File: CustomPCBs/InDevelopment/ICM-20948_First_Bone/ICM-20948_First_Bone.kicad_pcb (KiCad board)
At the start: 4 copper layers, 7 x 10.1 mm, 14 parts, among them J1 Conn_01x04_MountingPin, T1 BSS138BKS_115, U1 ICM-20948, U2 HE6206-18NR

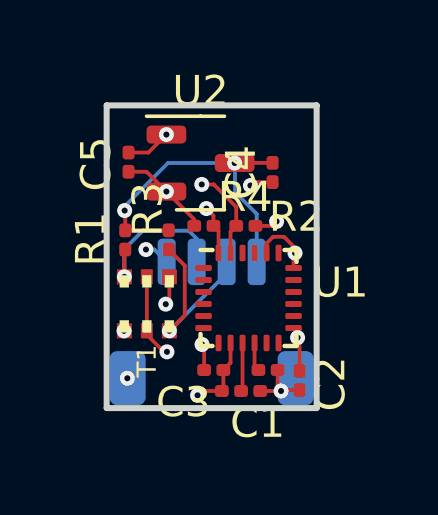
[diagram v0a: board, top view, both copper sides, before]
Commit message: BMI160+mag board finished, fixed CS on ICM-20948
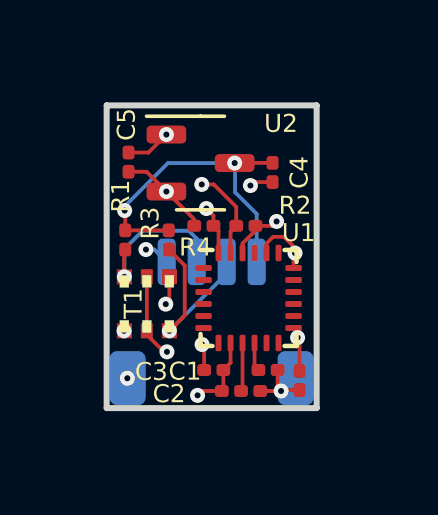
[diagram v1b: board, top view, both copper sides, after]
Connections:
- U1 pad 22: unconnected-(U1-~{CS}-Pad22) -> +1V8
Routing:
- net +1V8: track 10.8 -> 11.9 mm
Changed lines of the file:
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@@
   (net 23 "unconnected-(U1-RESV-Pad19)")
   (net 24 "unconnected-(U1-AUX_DA-Pad21)")
-  (net 25 "unconnected-(U1-~{CS}-Pad22)")
   (footprint "Capacitor_SMD:C_0201_0603Metric" (layer "F.Cu")
     (at 100.07 101.605)
@@
     (property "ki_keywords" "cap capacitor")
     (attr smd)
-    (fp_text reference "C3" (at -1.01 1.075) (layer "F.SilkS")
-        (effects (font (size 1 1) (thickness 0.15)))
+    (fp_text reference "C3" (at -2.08 0.055) (layer "F.SilkS")
+        (effects (font (size 0.6 0.6) (thickness 0.15)))
     )
     (fp_text value "100n" (at 0 1.05) (layer "F.Fab")
@@
     (property "ki_keywords" "R res resistor")
     (attr smd)
-    (fp_text reference "R1" (at -0.03 1.14 90) (layer "F.SilkS")
-        (effects (font (size 1 1) (thickness 0.15)))
+    (fp_text reference "R1" (at -1.46 0.15 90) (layer "F.SilkS")
+        (effects (font (size 0.6 0.6) (thickness 0.15)))
     )
     (fp_text value "10k" (at 0 1.05 90) (layer "F.Fab")
@@
     (property "ki_keywords" "R res resistor")
     (attr smd)
-    (fp_text reference "R4" (at 1.38 -0.96) (layer "F.SilkS")
-        (effects (font (size 1 1) (thickness 0.15)))
+    (fp_text reference "R4" (at -0.28 0.71) (layer "F.SilkS")
+        (effects (font (size 0.6 0.6) (thickness 0.15)))
     )
     (fp_text value "10k" (at 0 1.05) (layer "F.Fab")
@@
     (property "ki_keywords" "R res resistor")
     (attr smd)
-    (fp_text reference "R2" (at -1.68 0.3) (layer "F.SilkS")
-        (effects (font (size 1 1) (thickness 0.15)))
+    (fp_text reference "R2" (at -1.64 0.68) (layer "F.SilkS")
+        (effects (font (size 0.6 0.6) (thickness 0.15)))
     )
     (fp_text value "10k" (at 0 1.05) (layer "F.Fab")
@@
     (property "ki_keywords" "cap capacitor")
     (attr smd)
-    (fp_text reference "C2" (at 0.115 -1.03 90) (layer "F.SilkS")
-        (effects (font (size 1 1) (thickness 0.15)))
+    (fp_text reference "C2" (at 0.445 4.35 -180) (layer "F.SilkS")
+        (effects (font (size 0.6 0.6) (thickness 0.15)))
     )
     (fp_text value "100n" (at 0 1.05 90) (layer "F.Fab")
@@
     (property "ki_keywords" "mems magnetometer")
     (attr smd)
-    (fp_text reference "U1" (at 3.06 -0.51) (layer "F.SilkS")
-        (effects (font (size 1 1) (thickness 0.15)))
+    (fp_text reference "U1" (at 1.67 -2.175) (layer "F.SilkS")
+        (effects (font (size 0.6 0.6) (thickness 0.15)))
     )
     (fp_text value "ICM-20948" (at 0 3.25) (layer "F.Fab")
@@
       (net 24 "unconnected-(U1-AUX_DA-Pad21)") (pinfunction "AUX_DA") (pintype "bidirectional"))
     (pad "22" smd roundrect (at -0.2 -1.5 90) (size 0.55 0.2) (layers "F.Cu" "F.Paste" "F.Mask") (roundrect_rratio 0.25)
-      (net 25 "unconnected-(U1-~{CS}-Pad22)") (pinfunction "~{CS}") (pintype "input"))
+      (net 3 "+1V8") (pinfunction "~{CS}") (pintype "input"))
     (pad "23" smd roundrect (at -0.6 -1.5 90) (size 0.55 0.2) (layers "F.Cu" "F.Paste" "F.Mask") (roundrect_rratio 0.25)
       (net 7 "SCL_1V8") (pinfunction "SCL/SCLK") (pintype "input"))
@@
       )
     )
-    (model "${KICAD6_3DMODEL_DIR}/Package_DFN_QFN.3dshapes/QFN-24_3x3mm_P0.4mm_EP1.7x1.54mm.wrl"
-      (offset (xyz 0 0 0))
-      (scale (xyz 1 1 1))
-      (rotate (xyz 0 0 0))
+    (model ":REPO_ROOT:CustomPCBs/ComponentLibraries/3dmodels/ICM-20948.step"
+      (offset (xyz 0 0 0))
+      (scale (xyz 1 1 1))
+      (rotate (xyz -90 0 0))
     )
   )
@@
     (property "ki_keywords" "Torex LDO Voltage Regulator Fixed Positive")
     (attr smd)
-    (fp_text reference "U2" (at 0 -2.4) (layer "F.SilkS")
-        (effects (font (size 1 1) (thickness 0.15)))
+    (fp_text reference "U2" (at 2.68075 -1.31675) (layer "F.SilkS")
+        (effects (font (size 0.6 0.6) (thickness 0.15)))
     )
     (fp_text value "HE6206-18NR" (at 0 2.4) (layer "F.Fab")
@@
     (pad "3" smd roundrect (at 1.1375 0) (size 1.325 0.6) (layers "F.Cu" "F.Paste" "F.Mask") (roundrect_rratio 0.25)
       (net 4 "+3.3V") (pinfunction "VI") (pintype "power_in"))
-    (model "${KICAD6_3DMODEL_DIR}/Package_TO_SOT_SMD.3dshapes/SOT-23-3.wrl"
-      (offset (xyz 0 0 0))
-      (scale (xyz 1 1 1))
-      (rotate (xyz 0 0 0))
+    (model ":REPO_ROOT:CustomPCBs/ComponentLibraries/3dmodels/User Library-SOT23-3.step"
+      (offset (xyz 0 0 0))
+      (scale (xyz 1 1 1))
+      (rotate (xyz 0 0 90))
     )
   )
@@
     (property "ki_keywords" "cap capacitor")
     (attr smd)
-    (fp_text reference "C5" (at 0.06 1.08 90) (layer "F.SilkS")
-        (effects (font (size 1 1) (thickness 0.15)))
+    (fp_text reference "C5" (at -1.25675 0.06925 90) (layer "F.SilkS")
+        (effects (font (size 0.6 0.6) (thickness 0.15)))
     )
     (fp_text value "1u" (at 0 1.05 90) (layer "F.Fab")
@@
     (property "SnapEDA_Link" "https://www.snapeda.com/parts/BSS138BKS,115/Nexperia/view-part/?ref=snap")
     (attr smd)
-    (fp_text reference "T1" (at -1.90803 0 90) (layer "F.SilkS")
-        (effects (font (size 0.641017 0.641017) (thickness 0.15)))
+    (fp_text reference "T1" (at 0.01 -0.45 90) (layer "F.SilkS")
+        (effects (font (size 0.6 0.6) (thickness 0.15)))
     )
     (fp_text value "BSS138BKS_115" (at 1.90726 0 90) (layer "F.Fab")
@@
     (pad "6" smd roundrect (at 0.9 -0.75) (size 0.5 0.5) (layers "F.Cu" "F.Paste" "F.Mask") (roundrect_rratio 0.03)
       (net 6 "SCL") (pintype "passive") (solder_mask_margin 0.102))
+    (model ":REPO_ROOT:CustomPCBs/ComponentLibraries/3dmodels/User Library-TSSOP-6 (SOT-23-6 PITCH 0_65).STEP"
+      (offset (xyz 0 0 0.75))
+      (scale (xyz 1 1 1))
+      (rotate (xyz 0 0 -90))
+    )
   )
   (footprint "Resistor_SMD:R_0201_0603Metric" (layer "F.Cu")
@@
     (property "ki_keywords" "R res resistor")
     (attr smd)
-    (fp_text reference "R3" (at -1.02 0.7 90) (layer "F.SilkS")
-        (effects (font (size 1 1) (thickness 0.15)))
+    (fp_text reference "R3" (at -0.56 0.62 90) (layer "F.SilkS")
+        (effects (font (size 0.6 0.6) (thickness 0.15)))
     )
     (fp_text value "10k" (at 0 1.05 90) (layer "F.Fab")
@@
     (property "ki_keywords" "cap capacitor")
     (attr smd)
-    (fp_text reference "C4" (at 0 -1.05 90) (layer "F.SilkS")
-        (effects (font (size 1 1) (thickness 0.15)))
+    (fp_text reference "C4" (at 0 0.89 90) (layer "F.SilkS")
+        (effects (font (size 0.6 0.6) (thickness 0.15)))
     )
     (fp_text value "1u" (at 0 1.05 90) (layer "F.Fab")
@@
     (property "ki_keywords" "cap capacitor")
     (attr smd)
-    (fp_text reference "C1" (at -0.35 1.765) (layer "F.SilkS")
-        (effects (font (size 1 1) (thickness 0.15)))
+    (fp_text reference "C1" (at -2.77 0.045) (layer "F.SilkS")
+        (effects (font (size 0.6 0.6) (thickness 0.15)))
     )
     (fp_text value "100n" (at 0 1.05) (layer "F.Fab")
@@
     (pad "MP" smd roundrect (at 2.8 -1.875 180) (size 1.2 1.8) (layers "B.Cu" "B.Paste" "B.Mask") (roundrect_rratio 0.208333)
       (net 2 "GND") (pinfunction "MountPin") (pintype "passive"))
-    (model "${KICAD6_3DMODEL_DIR}/Connector_JST.3dshapes/JST_SH_SM04B-SRSS-TB_1x04-1MP_P1.00mm_Horizontal.wrl"
-      (offset (xyz 0 0 0))
-      (scale (xyz 1 1 1))
-      (rotate (xyz 0 0 0))
+    (model ":REPO_ROOT:CustomPCBs/ComponentLibraries/3dmodels/SM04B-SRSS-TB.STEP"
+      (offset (xyz 0 1.35 -0.35))
+      (scale (xyz 1 1 1))
+      (rotate (xyz -90 0 0))
     )
   )
@@
   (segment (start 97.195 101.875) (end 97.19 101.88) (width 0.127) (layer "B.Cu") (net 2))
   (segment (start 100.39 101.605) (end 100.63 101.365) (width 0.127) (layer "F.Cu") (net 3))
+  (segment (start 101.46 96.8) (end 101.46 96.955258) (width 0.127) (layer "F.Cu") (net 3))
   (segment (start 99.42 96.585) (end 99.42 96.8) (width 0.127) (layer "F.Cu") (net 3))
   (segment (start 98.4095 100.9995) (end 97.84 100.43) (width 0.127) (layer "F.Cu") (net 3))
   (segment (start 102.93 101.635) (end 102.93 100.590717) (width 0.127) (layer "F.Cu") (net 3))
+  (segment (start 101.46 96.955258) (end 101.03 97.385258) (width 0.127) (layer "F.Cu") (net 3))
+  (segment (start 101.03 97.385258) (end 101.03 97.705) (width 0.127) (layer "F.Cu") (net 3))
   (segment (start 102.864783 100.339783) (end 102.73 100.205) (width 0.127) (layer "F.Cu") (net 3))
   (segment (start 98.49175 95.65675) (end 99.42 96.585) (width 0.127) (layer "F.Cu") (net 3))
